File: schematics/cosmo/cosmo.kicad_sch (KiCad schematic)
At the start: 13 parts, among them M1 Motor_DC, SW1 SW_Push, U1 Rust_Board, U2 DRV8833PW, U3 ITR20001-T, U4 ITR20001-T, U5 ITR20001-T, U6 ITR20001-T

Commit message: Remove unnecessary pull down resistors and wrong connection to VCC
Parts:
- removed R2, R3, R4, R5: 10k, symbol Device:R
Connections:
- net +5V: no longer R1.1, U3.2 (A), U4.2 (A), U5.2 (A), U6.2 (A)
- new net: R1.1, U3.2 (A), U4.2 (A), U5.2 (A), U6.2 (A)

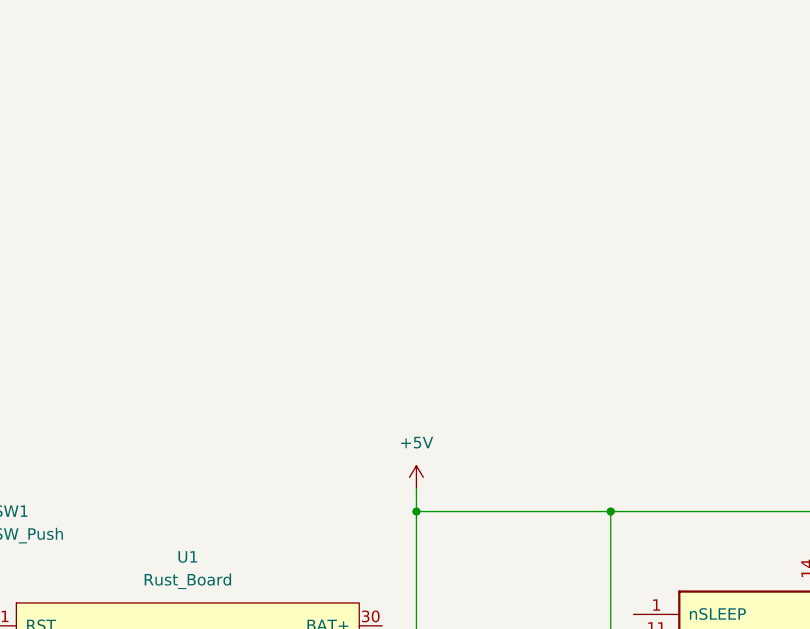
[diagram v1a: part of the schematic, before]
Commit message: Add separate connector schematic
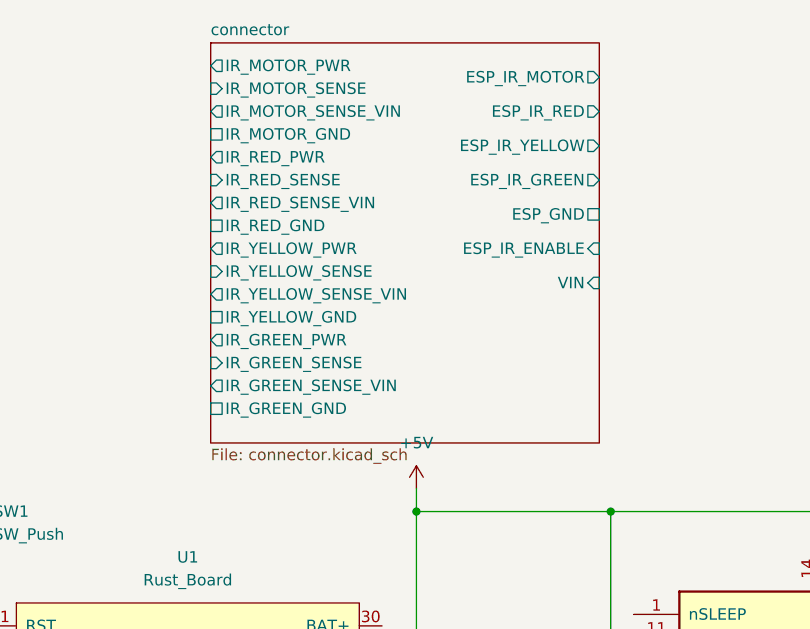
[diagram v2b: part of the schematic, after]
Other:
- added sheet connector (connector.kicad_sch)
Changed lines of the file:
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@@
     (pin "1")
+  )
+  (sheet (at 153.67 17.78) (size 43.18 44.45) (fields_autoplaced)
+    (stroke (width 0.1524) (type solid) (color 0 0 0 0))
+    (fill (color 0 0 0 0.0000))
+    (property "Sheet name" "connector" (id 0) (at 153.67 17.0684 0)
+      (effects (font (size 1.27 1.27)) (justify left bottom))
+    )
+    (property "Sheet file" "connector.kicad_sch" (id 1) (at 153.67 62.8146 0)
+      (effects (font (size 1.27 1.27)) (justify left top))
+    )
+    (pin "ESP_IR_MOTOR" output (at 196.85 21.59 0)
+      (effects (font (size 1.27 1.27)) (justify right))
+    )
+    (pin "ESP_IR_RED" output (at 196.85 25.4 0)
+      (effects (font (size 1.27 1.27)) (justify right))
+    )
+    (pin "ESP_IR_YELLOW" output (at 196.85 29.21 0)
+      (effects (font (size 1.27 1.27)) (justify right))
+    )
+    (pin "ESP_IR_GREEN" output (at 196.85 33.02 0)
+      (effects (font (size 1.27 1.27)) (justify right))
+    )
+    (pin "ESP_GND" passive (at 196.85 36.83 0)
+      (effects (font (size 1.27 1.27)) (justify right))
+    )
+    (pin "ESP_IR_ENABLE" input (at 196.85 40.64 0)
+      (effects (font (size 1.27 1.27)) (justify right))
+    )
+    (pin "IR_GREEN_GND" passive (at 153.67 58.42 180)
+      (effects (font (size 1.27 1.27)) (justify left))
+    )
+    (pin "IR_GREEN_PWR" output (at 153.67 50.8 180)
+      (effects (font (size 1.27 1.27)) (justify left))
+    )
+    (pin "IR_YELLOW_GND" passive (at 153.67 48.26 180)
+      (effects (font (size 1.27 1.27)) (justify left))
+    )
+    (pin "IR_YELLOW_SENSE" input (at 153.67 43.18 180)
+      (effects (font (size 1.27 1.27)) (justify left))
+    )
+    (pin "IR_GREEN_SENSE" input (at 153.67 53.34 180)
+      (effects (font (size 1.27 1.27)) (justify left))
+    )
+    (pin "IR_MOTOR_GND" passive (at 153.67 27.94 180)
+      (effects (font (size 1.27 1.27)) (justify left))
+    )
+    (pin "IR_RED_SENSE" input (at 153.67 33.02 180)
+      (effects (font (size 1.27 1.27)) (justify left))
+    )
+    (pin "IR_RED_GND" passive (at 153.67 38.1 180)
+      (effects (font (size 1.27 1.27)) (justify left))
+    )
+    (pin "IR_RED_PWR" output (at 153.67 30.48 180)
+      (effects (font (size 1.27 1.27)) (justify left))
+    )
+    (pin "IR_YELLOW_PWR" output (at 153.67 40.64 180)
+      (effects (font (size 1.27 1.27)) (justify left))
+    )
+    (pin "IR_MOTOR_SENSE" input (at 153.67 22.86 180)
+      (effects (font (size 1.27 1.27)) (justify left))
+    )
+    (pin "IR_MOTOR_PWR" output (at 153.67 20.32 180)
+      (effects (font (size 1.27 1.27)) (justify left))
+    )
+    (pin "IR_MOTOR_SENSE_VIN" output (at 153.67 25.4 180)
+      (effects (font (size 1.27 1.27)) (justify left))
+    )
+    (pin "IR_RED_SENSE_VIN" output (at 153.67 35.56 180)
+      (effects (font (size 1.27 1.27)) (justify left))
+    )
+    (pin "VIN" input (at 196.85 44.45 0)
+      (effects (font (size 1.27 1.27)) (justify right))
+    )
+    (pin "IR_YELLOW_SENSE_VIN" output (at 153.67 45.72 180)
+      (effects (font (size 1.27 1.27)) (justify left))
+    )
+    (pin "IR_GREEN_SENSE_VIN" output (at 153.67 55.88 180)
+      (effects (font (size 1.27 1.27)) (justify left))
+    )
   )
   (sheet_instances
     (path "/" (page "1"))
+    (path "/f85636ca-aeea-4617-a99d-06f43d374971" (page "2"))
   )
   (symbol_instances
     (path "/19383e60-3941-4263-b876-75a30056028e"
+      (reference "#PWR?") (unit 1) (value "GND") (footprint "")
+    )
+    (path "/f85636ca-aeea-4617-a99d-06f43d374971/1d818339-5d50-48f2-a223-0d1e6e295b17"
       (reference "#PWR?") (unit 1) (value "GND") (footprint "")
     )
@@
       (reference "M1") (unit 1) (value "Motor_DC") (footprint "")
     )
+    (path "/f85636ca-aeea-4617-a99d-06f43d374971/11db9a20-b327-4dc4-98f2-6424cd9e4f6a"
+      (reference "R1") (unit 1) (value "100") (footprint "")
+    )
     (path "/511b5429-a411-4cfc-a802-2c8cab87e54f"
       (reference "R1") (unit 1) (value "330") (footprint "")
     )
+    (path "/f85636ca-aeea-4617-a99d-06f43d374971/e331abe5-a7d5-4228-8fc7-aa327b594242"
+      (reference "RV1") (unit 1) (value "500") (footprint "")
+    )
+    (path "/f85636ca-aeea-4617-a99d-06f43d374971/087788e0-7fc7-47b2-9f31-976a89a9865b"
+      (reference "RV2") (unit 1) (value "500") (footprint "")
+    )
+    (path "/f85636ca-aeea-4617-a99d-06f43d374971/81ab71d3-a272-43f1-b179-752a2cb75667"
+      (reference "RV3") (unit 1) (value "500") (footprint "")
+    )
+    (path "/f85636ca-aeea-4617-a99d-06f43d374971/f9cc522e-bdbc-4c91-a42a-6af7963a9877"
+      (reference "RV4") (unit 1) (value "500") (footprint "")
+    )
     (path "/d0cd19f5-c4b4-4347-9b42-f5076fdab82d"

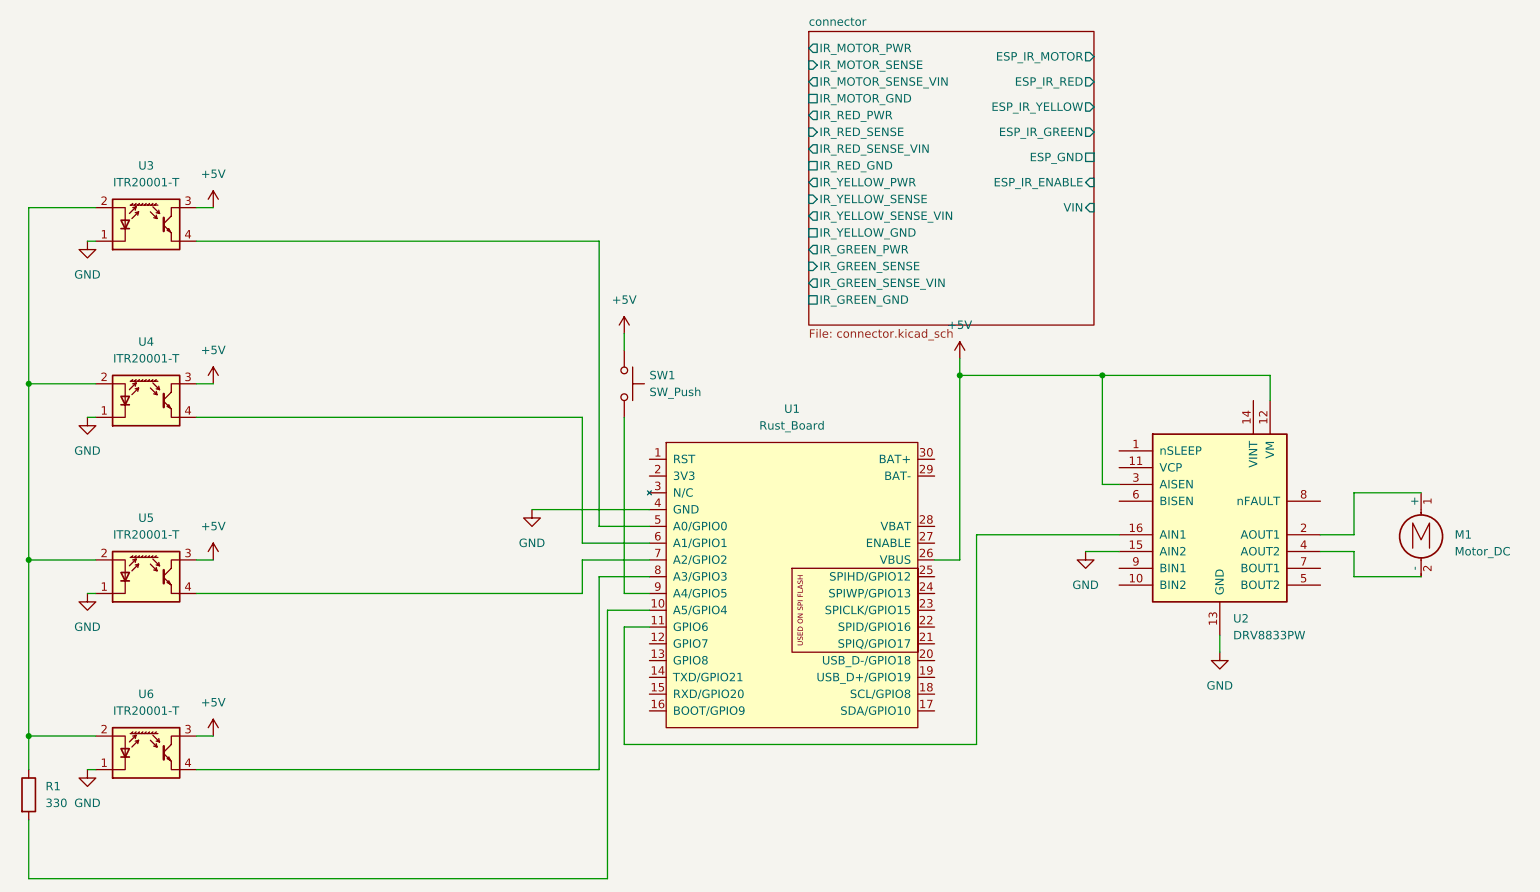
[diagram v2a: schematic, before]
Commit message: Add PD resistors to sense pins, integrate connector into main schematic
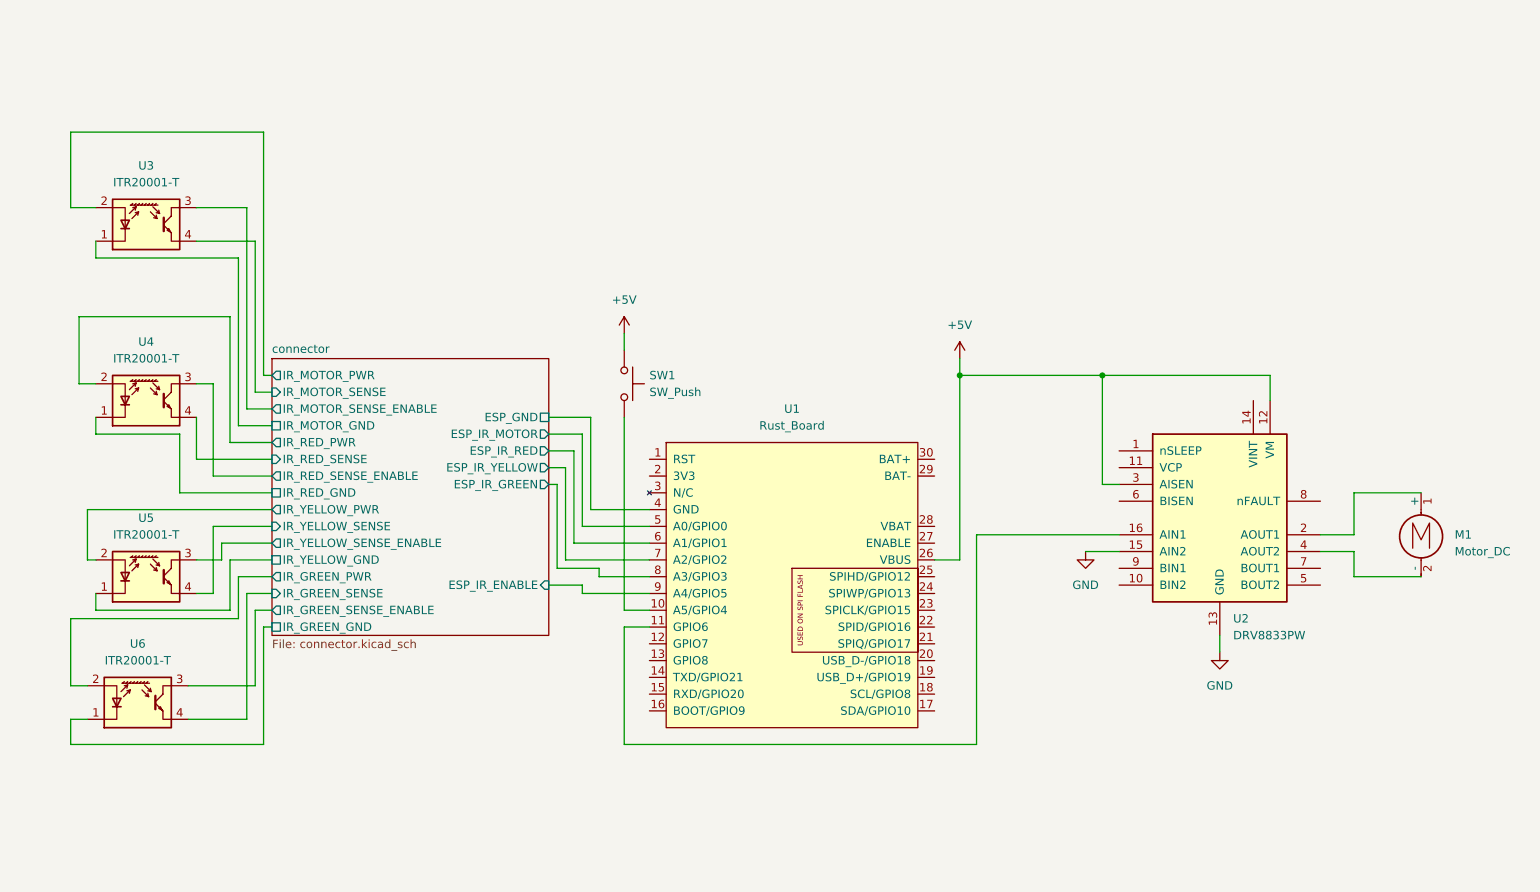
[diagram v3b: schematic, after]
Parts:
- removed R1: 330, symbol Device:R
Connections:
- net +5V: no longer U3.3, U4.3, U5.3, U6.3
- net GND: no longer U1.4 (GND), U3.1 (K), U4.1 (K), U5.1 (K), U6.1 (K)
- net connector/ESP_GND: now also U1.4 (GND)
- net connector/ESP_IR_ENABLE: now also U1.9 (A4/GPIO5)
- net connector/ESP_IR_GREEN: now also U1.8 (A3/GPIO3)
- net connector/ESP_IR_MOTOR: now also U1.5 (A0/GPIO0)
- net connector/ESP_IR_RED: now also U1.6 (A1/GPIO1)
- net connector/ESP_IR_YELLOW: now also U1.7 (A2/GPIO2)
- net connector/IR_GREEN_GND: now also U6.1 (K)
- net connector/IR_GREEN_PWR: now also U6.2 (A)
- net connector/IR_GREEN_SENSE: now also U6.4
- net connector/IR_MOTOR_GND: now also U3.1 (K)
- net connector/IR_MOTOR_PWR: now also U3.2 (A)
- net connector/IR_MOTOR_SENSE: now also U3.4
- net connector/IR_RED_GND: now also U4.1 (K)
- net connector/IR_RED_PWR: now also U4.2 (A)
- net connector/IR_RED_SENSE: now also U4.4
- net connector/IR_YELLOW_GND: now also U5.1 (K)
- net connector/IR_YELLOW_PWR: now also U5.2 (A)
- net connector/IR_YELLOW_SENSE: now also U5.4
- net at U1.10 (A5/GPIO4): now also SW1.2
- new net connector/IR_GREEN_SENSE_ENABLE: U6.3
- new net connector/IR_MOTOR_SENSE_ENABLE: U3.3
- new net connector/IR_RED_SENSE_ENABLE: U4.3
- new net connector/IR_YELLOW_SENSE_ENABLE: U5.3
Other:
- sheet connector ports: added IR_GREEN_SENSE_ENABLE, IR_MOTOR_SENSE_ENABLE, IR_RED_SENSE_ENABLE, IR_YELLOW_SENSE_ENABLE; removed IR_GREEN_SENSE_VIN, IR_MOTOR_SENSE_VIN, IR_RED_SENSE_VIN, IR_YELLOW_SENSE_VIN, VIN
- moved on the sheet: U6

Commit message: Select connector footprints (WIP)
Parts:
- M1, SW1: footprint (none) -> Connector_PinHeader_2.54mm:PinHeader_1x02_P2.54mm_Vertical
- U3, U4, U5, U6: footprint OptoDevice:Everlight_ITR1201SR10AR -> Connector_PinHeader_2.54mm:PinHeader_1x02_P2.54mm_Vertical
